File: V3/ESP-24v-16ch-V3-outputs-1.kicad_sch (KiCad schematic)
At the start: 80 parts, among them Q10 MMBT2222A/SOT-23-3, Q11 MMBT2222A/SOT-23-3, Q12 MMBT2222A/SOT-23-3, Q13 MMBT2222A/SOT-23-3, Q14 MMBT2222A/SOT-23-3, Q15 MMBT2222A/SOT-23-3, Q16 MMBT2222A/SOT-23-3, Q17 MMBT2222A/SOT-23-3, Q18 MMBT2222A/SOT-23-3, Q19 MMBT2222A/SOT-23-3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

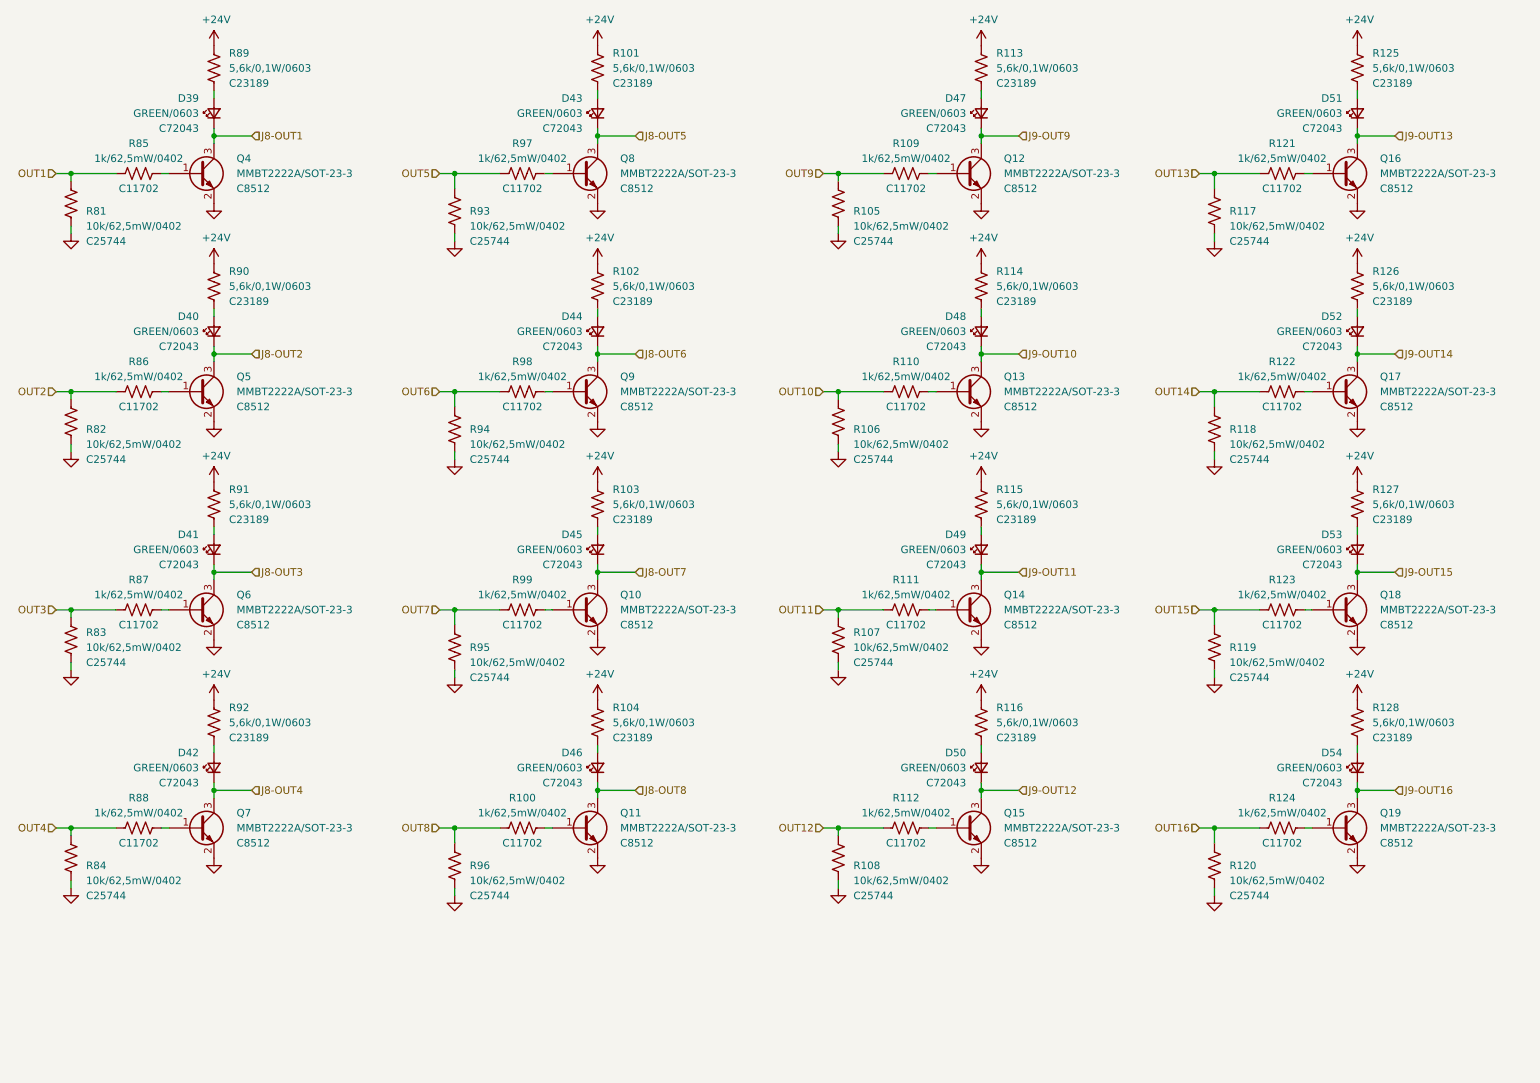
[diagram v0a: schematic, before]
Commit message: Replaced R16 and R17 for a R-Pack
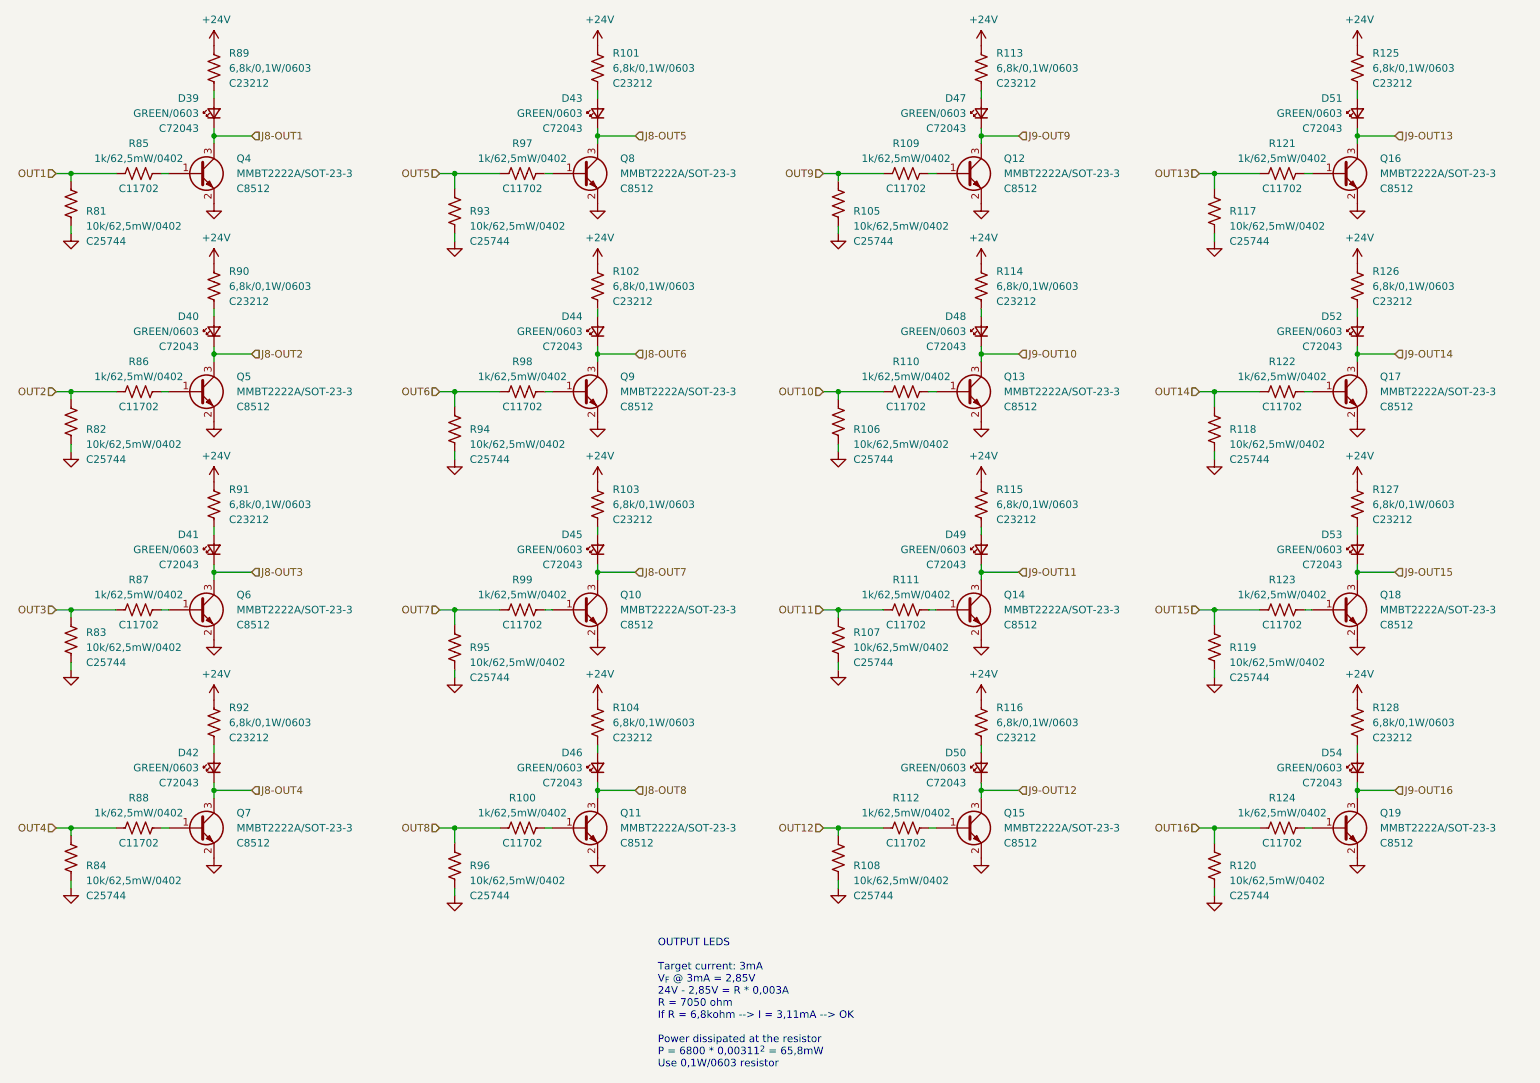
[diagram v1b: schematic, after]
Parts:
- R101, R102, R103, R104, R113, R114, R115, R116, R125, R126, R127, R128, R89, R90, R91, R92: value 5,6k/0,1W/0603 -> 6,8k/0,1W/0603; LCSC Part # C23189 -> C23212; Mfr PN 0603WAF5601T5E -> 0603WAF6801T5E; Vendor PN C23189 -> C23212
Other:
- note added: "OUTPUT LEDS Target current: 3mA V_{F} @ 3mA = 2,85V 24V - 2,85V = R * 0,003A R = 7050 ohm If R = 6,8kohm --> I = 3,11mA --> OK Power dissipated at the resistor P = 6800 * 0,00311^{2} = 65,8mW Use 0,1W/0603 resistor"
